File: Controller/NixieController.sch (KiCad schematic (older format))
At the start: 22 parts, among them J1 Conn_01x12_Male, J2 Conn_01x12_Male, J3 Conn_01x12_Male, J4 Conn_01x12_Male, J5 Conn_01x12_Male, J6 Conn_01x12_Male, J7 Jack-DC, J8 Conn_01x02_Male, J9 Conn_01x06_Male, U1 ATtiny85-20SU, U10 74HC595, U11 74HC595, U12 74HC595, U2 DS1307Z+, U5 74HC595, U6 74HC595, U7 74HC595, U8 74HC595, U9 74HC595, Y1 32.768kHz

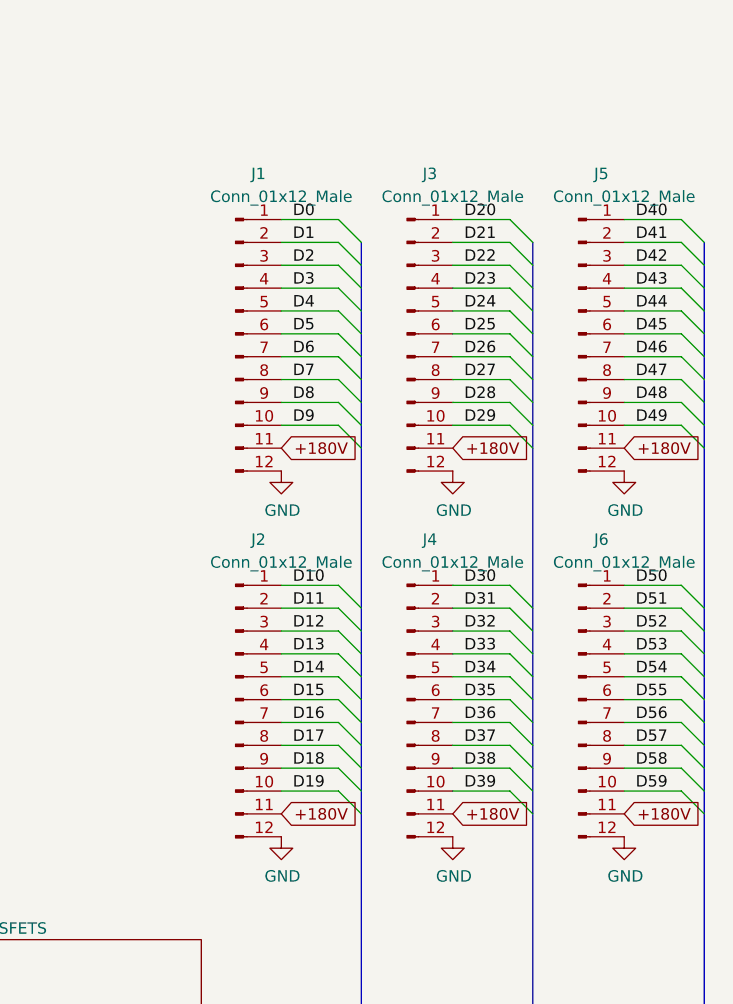
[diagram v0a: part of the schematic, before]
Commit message: Change pin header on controller from male to female
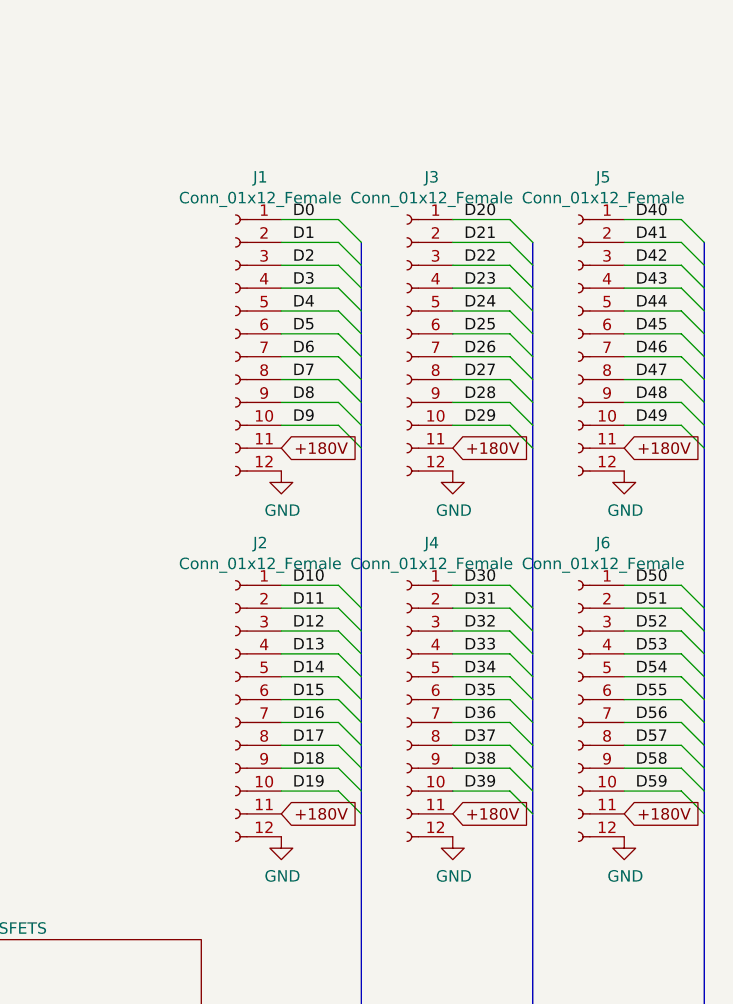
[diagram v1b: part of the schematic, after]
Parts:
- removed J1, J2, J3, J4, J5, J6: Conn_01x12_Male, Connector_PinHeader_2.54mm:PinHeader_1x12_P2.54mm_Vertical, symbol Connector:Conn_01x12_Male
- added J1, J2, J3, J4, J5, J6: Conn_01x12_Female, Connector_PinSocket_2.54mm:PinSocket_1x12_P2.54mm_Vertical, symbol Connector:Conn_01x12_Female
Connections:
- net +180V: now also J1.11 (Pin_11), J2.11 (Pin_11), J3.11 (Pin_11), J4.11 (Pin_11), J5.11 (Pin_11), J6.11 (Pin_11)
- net D0: now also J1.1 (Pin_1)
- net D1: now also J1.2 (Pin_2)
- net D10: now also J2.1 (Pin_1)
- net D11: now also J2.2 (Pin_2)
- net D12: now also J2.3 (Pin_3)
- net D13: now also J2.4 (Pin_4)
- net D14: now also J2.5 (Pin_5)
- net D15: now also J2.6 (Pin_6)
- net D16: now also J2.7 (Pin_7)
- net D17: now also J2.8 (Pin_8)
- net D18: now also J2.9 (Pin_9)
- net D19: now also J2.10 (Pin_10)
- net D2: now also J1.3 (Pin_3)
- net D20: now also J3.1 (Pin_1)
- net D21: now also J3.2 (Pin_2)
- net D22: now also J3.3 (Pin_3)
- net D23: now also J3.4 (Pin_4)
- net D24: now also J3.5 (Pin_5)
- net D25: now also J3.6 (Pin_6)
- net D26: now also J3.7 (Pin_7)
- net D27: now also J3.8 (Pin_8)
- net D28: now also J3.9 (Pin_9)
- net D29: now also J3.10 (Pin_10)
- net D3: now also J1.4 (Pin_4)
- net D30: now also J4.1 (Pin_1)
- net D31: now also J4.2 (Pin_2)
- net D32: now also J4.3 (Pin_3)
- net D33: now also J4.4 (Pin_4)
- net D34: now also J4.5 (Pin_5)
- net D35: now also J4.6 (Pin_6)
- net D36: now also J4.7 (Pin_7)
- net D37: now also J4.8 (Pin_8)
- net D38: now also J4.9 (Pin_9)
- net D39: now also J4.10 (Pin_10)
- net D4: now also J1.5 (Pin_5)
- net D40: now also J5.1 (Pin_1)
- net D41: now also J5.2 (Pin_2)
- net D42: now also J5.3 (Pin_3)
- net D43: now also J5.4 (Pin_4)
- net D44: now also J5.5 (Pin_5)
- net D45: now also J5.6 (Pin_6)
- net D46: now also J5.7 (Pin_7)
- net D47: now also J5.8 (Pin_8)
- net D48: now also J5.9 (Pin_9)
- net D49: now also J5.10 (Pin_10)
- net D5: now also J1.6 (Pin_6)
- net D50: now also J6.1 (Pin_1)
- net D51: now also J6.2 (Pin_2)
- net D52: now also J6.3 (Pin_3)
- net D53: now also J6.4 (Pin_4)
- net D54: now also J6.5 (Pin_5)
- net D55: now also J6.6 (Pin_6)
- net D56: now also J6.7 (Pin_7)
- net D57: now also J6.8 (Pin_8)
- net D58: now also J6.9 (Pin_9)
- net D59: now also J6.10 (Pin_10)
- net D6: now also J1.7 (Pin_7)
- net D7: now also J1.8 (Pin_8)
- net D8: now also J1.9 (Pin_9)
- net D9: now also J1.10 (Pin_10)
- net GND: now also J1.12 (Pin_12), J2.12 (Pin_12), J3.12 (Pin_12), J4.12 (Pin_12), J5.12 (Pin_12), J6.12 (Pin_12)
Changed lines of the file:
@@
 Wire Bus Line
 	7100 6200 7800 6200
-$Comp
-L Connector:Conn_01x12_Male J1
-U 1 1 5EDD0110
-P 8950 2750
-F 0 "J1" H 9050 3450 50  0000 C CNN
-F 1 "Conn_01x12_Male" H 9150 3350 50  0000 C CNN
-F 2 "Connector_PinHeader_2.54mm:PinHeader_1x12_P2.54mm_Vertical" H 8950 2750 50  0001 C CNN
-F 3 "~" H 8950 2750 50  0001 C CNN
-	1    8950 2750
-	1    0    0    -1
-$EndComp
 Entry Wire Line
 	9500 2350 9400 2250
@@
 Text GLabel 9150 3250 2    50   Input ~ 0
 +180V
-$Comp
-L Connector:Conn_01x12_Male J3
-U 1 1 5EDEC106
-P 9700 2750
-F 0 "J3" H 9800 3450 50  0000 C CNN
-F 1 "Conn_01x12_Male" H 9900 3350 50  0000 C CNN
-F 2 "Connector_PinHeader_2.54mm:PinHeader_1x12_P2.54mm_Vertical" H 9700 2750 50  0001 C CNN
-F 3 "~" H 9700 2750 50  0001 C CNN
-	1    9700 2750
-	1    0    0    -1
-$EndComp
 Entry Wire Line
 	10250 2350 10150 2250
@@
 Text GLabel 9900 3250 2    50   Input ~ 0
 +180V
-$Comp
-L Connector:Conn_01x12_Male J5
-U 1 1 5EDF1EB9
-P 10450 2750
-F 0 "J5" H 10550 3450 50  0000 C CNN
-F 1 "Conn_01x12_Male" H 10650 3350 50  0000 C CNN
-F 2 "Connector_PinHeader_2.54mm:PinHeader_1x12_P2.54mm_Vertical" H 10450 2750 50  0001 C CNN
-F 3 "~" H 10450 2750 50  0001 C CNN
-	1    10450 2750
-	1    0    0    -1
-$EndComp
 Entry Wire Line
 	11000 2350 10900 2250
@@
 Text GLabel 10650 3250 2    50   Input ~ 0
 +180V
-$Comp
-L Connector:Conn_01x12_Male J2
-U 1 1 5EE197E2
-P 8950 4350
-F 0 "J2" H 9050 5050 50  0000 C CNN
-F 1 "Conn_01x12_Male" H 9150 4950 50  0000 C CNN
-F 2 "Connector_PinHeader_2.54mm:PinHeader_1x12_P2.54mm_Vertical" H 8950 4350 50  0001 C CNN
-F 3 "~" H 8950 4350 50  0001 C CNN
-	1    8950 4350
-	1    0    0    -1
-$EndComp
 Entry Wire Line
 	9500 3950 9400 3850
@@
 Text GLabel 9150 4850 2    50   Input ~ 0
 +180V
-$Comp
-L Connector:Conn_01x12_Male J4
-U 1 1 5EE19803
-P 9700 4350
-F 0 "J4" H 9800 5050 50  0000 C CNN
-F 1 "Conn_01x12_Male" H 9900 4950 50  0000 C CNN
-F 2 "Connector_PinHeader_2.54mm:PinHeader_1x12_P2.54mm_Vertical" H 9700 4350 50  0001 C CNN
-F 3 "~" H 9700 4350 50  0001 C CNN
-	1    9700 4350
-	1    0    0    -1
-$EndComp
 Entry Wire Line
 	10250 3950 10150 3850
@@
 Text GLabel 9900 4850 2    50   Input ~ 0
 +180V
-$Comp
-L Connector:Conn_01x12_Male J6
-U 1 1 5EE19824
-P 10450 4350
-F 0 "J6" H 10550 5050 50  0000 C CNN
-F 1 "Conn_01x12_Male" H 10650 4950 50  0000 C CNN
-F 2 "Connector_PinHeader_2.54mm:PinHeader_1x12_P2.54mm_Vertical" H 10450 4350 50  0001 C CNN
-F 3 "~" H 10450 4350 50  0001 C CNN
-	1    10450 4350
-	1    0    0    -1
-$EndComp
 Entry Wire Line
 	11000 3950 10900 3850
@@
 Text Label 3950 1450 0    50   ~ 0
 RST
+$Comp
+L Connector:Conn_01x12_Female J1
+U 1 1 5EAD5BBD
+P 8950 2750
+F 0 "J1" H 8842 3435 50  0000 C CNN
+F 1 "Conn_01x12_Female" H 8842 3344 50  0000 C CNN
+F 2 "Connector_PinSocket_2.54mm:PinSocket_1x12_P2.54mm_Vertical" H 8950 2750 50  0001 C CNN
+F 3 "~" H 8950 2750 50  0001 C CNN
+	1    8950 2750
+	-1   0    0    -1
+$EndComp
+$Comp
+L Connector:Conn_01x12_Female J3
+U 1 1 5EADB596
+P 9700 2750
+F 0 "J3" H 9592 3435 50  0000 C CNN
+F 1 "Conn_01x12_Female" H 9592 3344 50  0000 C CNN
+F 2 "Connector_PinSocket_2.54mm:PinSocket_1x12_P2.54mm_Vertical" H 9700 2750 50  0001 C CNN
+F 3 "~" H 9700 2750 50  0001 C CNN
+	1    9700 2750
+	-1   0    0    -1
+$EndComp
+$Comp
+L Connector:Conn_01x12_Female J5
+U 1 1 5EAE7154
+P 10450 2750
+F 0 "J5" H 10342 3435 50  0000 C CNN
+F 1 "Conn_01x12_Female" H 10342 3344 50  0000 C CNN
+F 2 "Connector_PinSocket_2.54mm:PinSocket_1x12_P2.54mm_Vertical" H 10450 2750 50  0001 C CNN
+F 3 "~" H 10450 2750 50  0001 C CNN
+	1    10450 2750
+	-1   0    0    -1
+$EndComp
+$Comp
+L Connector:Conn_01x12_Female J6
+U 1 1 5EAF348B
+P 10450 4350
+F 0 "J6" H 10342 5035 50  0000 C CNN
+F 1 "Conn_01x12_Female" H 10342 4944 50  0000 C CNN
+F 2 "Connector_PinSocket_2.54mm:PinSocket_1x12_P2.54mm_Vertical" H 10450 4350 50  0001 C CNN
+F 3 "~" H 10450 4350 50  0001 C CNN
+	1    10450 4350
+	-1   0    0    -1
+$EndComp
+$Comp
+L Connector:Conn_01x12_Female J4
+U 1 1 5EAFF17E
+P 9700 4350
+F 0 "J4" H 9592 5035 50  0000 C CNN
+F 1 "Conn_01x12_Female" H 9592 4944 50  0000 C CNN
+F 2 "Connector_PinSocket_2.54mm:PinSocket_1x12_P2.54mm_Vertical" H 9700 4350 50  0001 C CNN
+F 3 "~" H 9700 4350 50  0001 C CNN
+	1    9700 4350
+	-1   0    0    -1
+$EndComp
+$Comp
+L Connector:Conn_01x12_Female J2
+U 1 1 5EB0B020
+P 8950 4350
+F 0 "J2" H 8842 5035 50  0000 C CNN
+F 1 "Conn_01x12_Female" H 8842 4944 50  0000 C CNN
+F 2 "Connector_PinSocket_2.54mm:PinSocket_1x12_P2.54mm_Vertical" H 8950 4350 50  0001 C CNN
+F 3 "~" H 8950 4350 50  0001 C CNN
+	1    8950 4350
+	-1   0    0    -1
+$EndComp
 Wire Bus Line
 	7100 3000 7100 6200

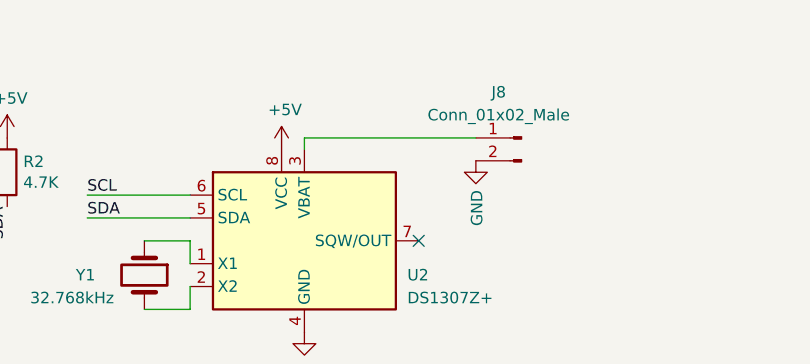
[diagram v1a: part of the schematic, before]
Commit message: Add battery mount to controller
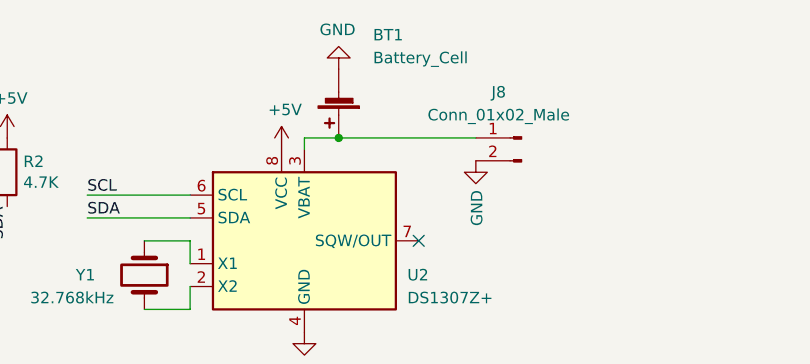
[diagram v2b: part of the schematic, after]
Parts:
- added BT1: Battery_Cell, NixieController:Keystone_1056, symbol Device:Battery_Cell
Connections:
- net GND: now also BT1.2 (-)
- net at J8.1 (Pin_1), U2.3 (VBAT): now also BT1.1 (+)
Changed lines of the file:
@@
 $EndComp
 Wire Wire Line
-	6250 1050 7000 1050
+	6250 1050 6400 1050
 Text Label 5300 1300 0    50   ~ 0
 SCL
@@
 	-1   0    0    -1
 $EndComp
+$Comp
+L Device:Battery_Cell BT1
+U 1 1 5EB21A49
+P 6400 850
+F 0 "BT1" H 6250 600 50  0000 R CNN
+F 1 "Battery_Cell" H 6250 700 50  0000 R CNN
+F 2 "NixieController:Keystone_1056" V 6400 910 50  0001 C CNN
+F 3 "~" V 6400 910 50  0001 C CNN
+	1    6400 850
+	-1   0    0    1
+$EndComp
+Connection ~ 6400 1050
+Wire Wire Line
+	6400 1050 7000 1050
+$Comp
+L power:GND #PWR016
+U 1 1 5EB25A64
+P 6400 750
+F 0 "#PWR016" H 6400 500 50  0001 C CNN
+F 1 "GND" H 6405 577 50  0000 C CNN
+F 2 "" H 6400 750 50  0001 C CNN
+F 3 "" H 6400 750 50  0001 C CNN
+	1    6400 750
+	-1   0    0    1
+$EndComp
 Wire Bus Line

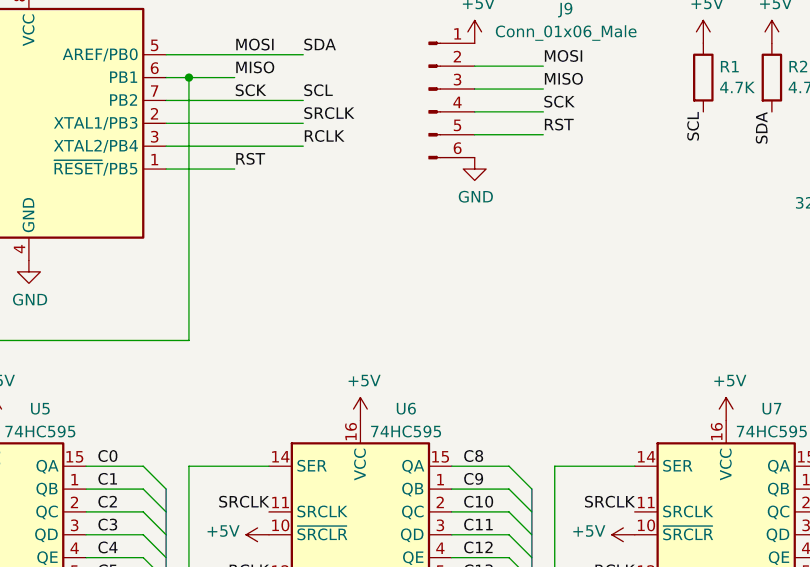
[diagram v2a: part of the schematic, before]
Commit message: Add bypass caps for micro and RTC
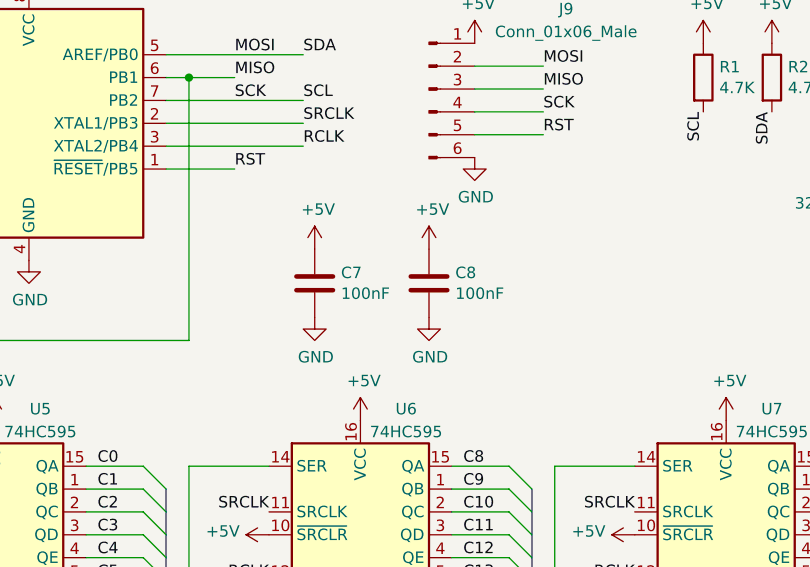
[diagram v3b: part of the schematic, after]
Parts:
- added C7, C8: 100nF, Capacitor_SMD:C_0805_2012Metric, symbol Device:C
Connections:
- net +5V: now also C7.1, C8.1
- net GND: now also C7.2, C8.2
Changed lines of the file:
@@
 	-1   0    0    1
+$EndComp
+$Comp
+L Device:C C?
+U 1 1 5EB8B6BF
+P 2950 2100
+AR Path="/5E933D65/5EB8B6BF" Ref="C?"  Part="1"
+AR Path="/5EB8B6BF" Ref="C7"  Part="1"
+F 0 "C7" H 3065 2146 50  0000 L CNN
+F 1 "100nF" H 3065 2055 50  0000 L CNN
+F 2 "Capacitor_SMD:C_0805_2012Metric" H 2988 1950 50  0001 C CNN
+F 3 "~" H 2950 2100 50  0001 C CNN
+	1    2950 2100
+	1    0    0    -1
+$EndComp
+$Comp
+L Device:C C?
+U 1 1 5EB96F42
+P 3450 2100
+AR Path="/5E933D65/5EB96F42" Ref="C?"  Part="1"
+AR Path="/5EB96F42" Ref="C8"  Part="1"
+F 0 "C8" H 3565 2146 50  0000 L CNN
+F 1 "100nF" H 3565 2055 50  0000 L CNN
+F 2 "Capacitor_SMD:C_0805_2012Metric" H 3488 1950 50  0001 C CNN
+F 3 "~" H 3450 2100 50  0001 C CNN
+	1    3450 2100
+	1    0    0    -1
+$EndComp
+$Comp
+L power:+5V #PWR017
+U 1 1 5EBA2F59
+P 2950 1950
+F 0 "#PWR017" H 2950 1800 50  0001 C CNN
+F 1 "+5V" H 2965 2123 50  0000 C CNN
+F 2 "" H 2950 1950 50  0001 C CNN
+F 3 "" H 2950 1950 50  0001 C CNN
+	1    2950 1950
+	1    0    0    -1
+$EndComp
+$Comp
+L power:+5V #PWR019
+U 1 1 5EBAEA35
+P 3450 1950
+F 0 "#PWR019" H 3450 1800 50  0001 C CNN
+F 1 "+5V" H 3465 2123 50  0000 C CNN
+F 2 "" H 3450 1950 50  0001 C CNN
+F 3 "" H 3450 1950 50  0001 C CNN
+	1    3450 1950
+	1    0    0    -1
+$EndComp
+$Comp
+L power:GND #PWR018
+U 1 1 5EBBAAAB
+P 2950 2250
+F 0 "#PWR018" H 2950 2000 50  0001 C CNN
+F 1 "GND" H 2955 2077 50  0000 C CNN
+F 2 "" H 2950 2250 50  0001 C CNN
+F 3 "" H 2950 2250 50  0001 C CNN
+	1    2950 2250
+	1    0    0    -1
+$EndComp
+$Comp
+L power:GND #PWR020
+U 1 1 5EBC64EB
+P 3450 2250
+F 0 "#PWR020" H 3450 2000 50  0001 C CNN
+F 1 "GND" H 3455 2077 50  0000 C CNN
+F 2 "" H 3450 2250 50  0001 C CNN
+F 3 "" H 3450 2250 50  0001 C CNN
+	1    3450 2250
+	1    0    0    -1
 $EndComp
 Wire Bus Line
